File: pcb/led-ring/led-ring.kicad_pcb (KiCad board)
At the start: 2 copper layers, 30 x 30 mm, 30 parts

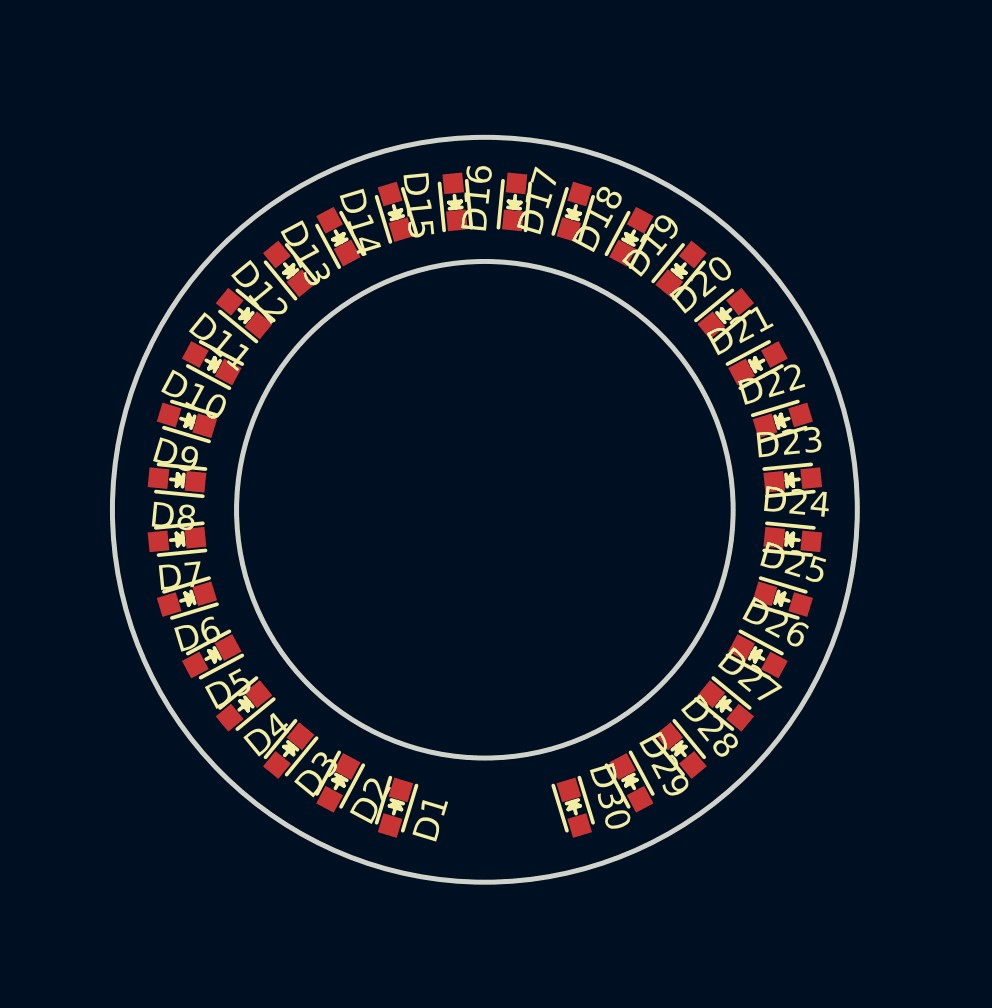
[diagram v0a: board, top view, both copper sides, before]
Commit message: o Add flat-flex footprint.
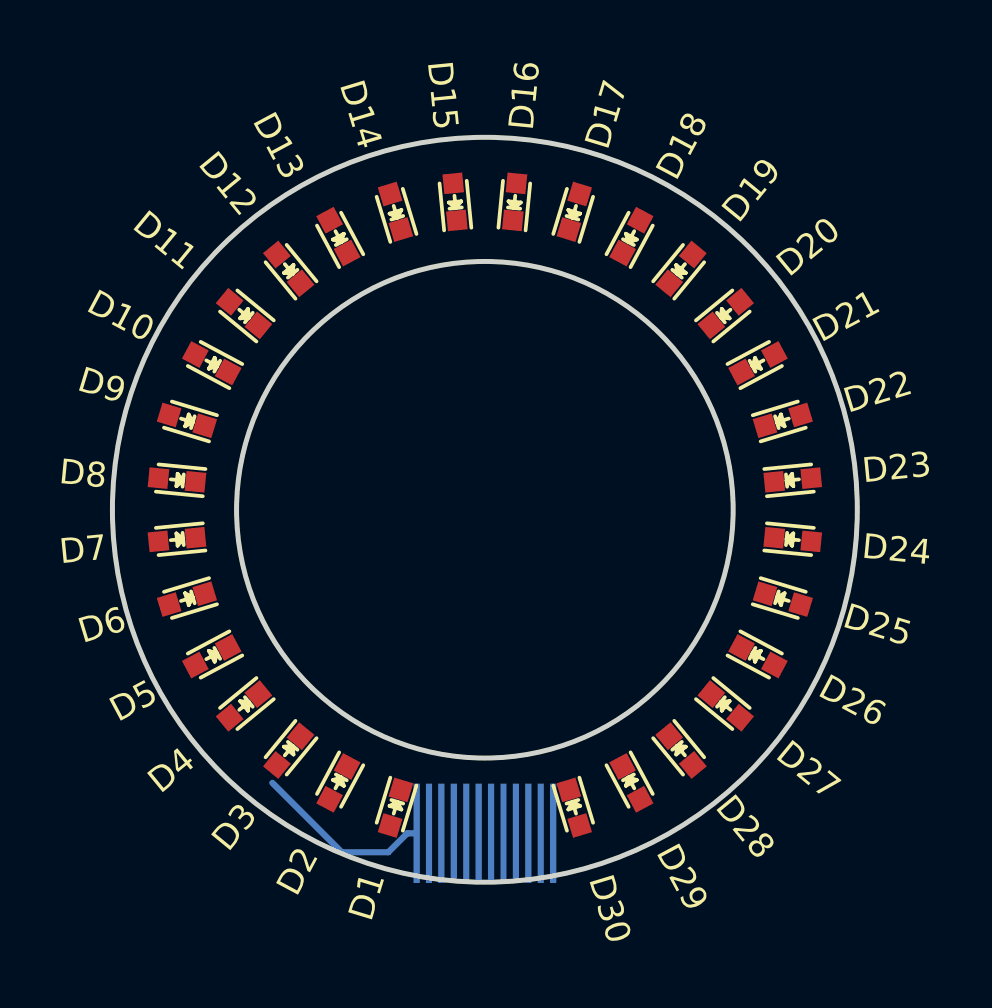
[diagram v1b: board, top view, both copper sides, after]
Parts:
- added P1: CONN_01X12, knopf:FlatFlex, B.Cu at (100.0, 113.0)
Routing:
- net A: track 0.00 -> 7.28 mm
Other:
- net class Default: clearance 0.2 -> 0.1
- rule trace_clearance: 0.2 -> 0.1

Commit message: o seed net-starts.
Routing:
- net C: track 0.00 -> 6.51 mm
- net B: track 0.00 -> 5.94 mm
- net A: track 7.28 -> 2.06 mm
- net D: track 0.00 -> 4.10 mm
- net E: track 0.00 -> 3.75 mm
- net F: track 0.00 -> 1.60 mm
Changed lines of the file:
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@@
     (links 60)
     (no_connects 60)
-    (area 84.899999 84.899999 115.100001 115.100001)
+    (area 82.586734 81.61799 118.293184 117.9685)
     (thickness 1.6)
     (drawings 2)
-    (tracks 4)
+    (tracks 25)
     (zones 0)
     (modules 31)
@@
   (gr_circle (center 100 100) (end 115 100) (layer Edge.Cuts) (width 0.2))
   (gr_circle (center 100 100) (end 110 100) (layer Edge.Cuts) (width 0.2))
-  (segment (start 94.234 113.792) (end 91.44 110.998) (width 0.25) (layer B.Cu) (net 1))
-  (segment (start 96.113 113.792) (end 94.234 113.792) (width 0.25) (layer B.Cu) (net 1))
+  (segment (start 96.113 113.792) (end 95.504 113.792) (width 0.25) (layer B.Cu) (net 1))
   (segment (start 97.25 113.03) (end 96.875 113.03) (width 0.25) (layer B.Cu) (net 1))
   (segment (start 96.875 113.03) (end 96.113 113.792) (width 0.25) (layer B.Cu) (net 1))
+  (segment (start 95.854011 111.895987) (end 95.854011 112.933989) (width 0.25) (layer B.Cu) (net 2))
+  (segment (start 95.854011 112.933989) (end 95.758 113.03) (width 0.25) (layer B.Cu) (net 2))
+  (segment (start 97.163987 110.586011) (end 95.854011 111.895987) (width 0.25) (layer B.Cu) (net 2))
+  (segment (start 97.556011 110.586011) (end 97.163987 110.586011) (width 0.25) (layer B.Cu) (net 2))
+  (segment (start 97.75 113.03) (end 97.75 110.78) (width 0.25) (layer B.Cu) (net 2))
+  (segment (start 97.75 110.78) (end 97.556011 110.586011) (width 0.25) (layer B.Cu) (net 2))
+  (segment (start 95.504 111.506) (end 95.504 112.268) (width 0.25) (layer B.Cu) (net 3))
+  (segment (start 96.774 110.236) (end 95.504 111.506) (width 0.25) (layer B.Cu) (net 3))
+  (segment (start 97.706 110.236) (end 96.774 110.236) (width 0.25) (layer B.Cu) (net 3))
+  (segment (start 98.25 113.03) (end 98.25 110.78) (width 0.25) (layer B.Cu) (net 3))
+  (segment (start 98.25 110.78) (end 97.706 110.236) (width 0.25) (layer B.Cu) (net 3))
+  (segment (start 102.294 110.236) (end 103.378 110.236) (width 0.25) (layer B.Cu) (net 4))
+  (segment (start 101.75 113.03) (end 101.75 110.78) (width 0.25) (layer B.Cu) (net 4))
+  (segment (start 101.75 110.78) (end 102.294 110.236) (width 0.25) (layer B.Cu) (net 4))
+  (segment (start 103.378 111.127998) (end 103.378 111.506) (width 0.25) (layer B.Cu) (net 5))
+  (segment (start 102.25 113.03) (end 102.25 110.999998) (width 0.25) (layer B.Cu) (net 5))
+  (segment (start 102.25 110.999998) (end 102.444999 110.804999) (width 0.25) (layer B.Cu) (net 5))
+  (segment (start 102.444999 110.804999) (end 103.055001 110.804999) (width 0.25) (layer B.Cu) (net 5))
+  (segment (start 103.055001 110.804999) (end 103.378 111.127998) (width 0.25) (layer B.Cu) (net 5))
+  (segment (start 103.632 112.523) (end 103.632 112.014) (width 0.25) (layer B.Cu) (net 6))
+  (segment (start 102.75 113.03) (end 103.125 113.03) (width 0.25) (layer B.Cu) (net 6))
+  (segment (start 103.125 113.03) (end 103.632 112.523) (width 0.25) (layer B.Cu) (net 6))
 )

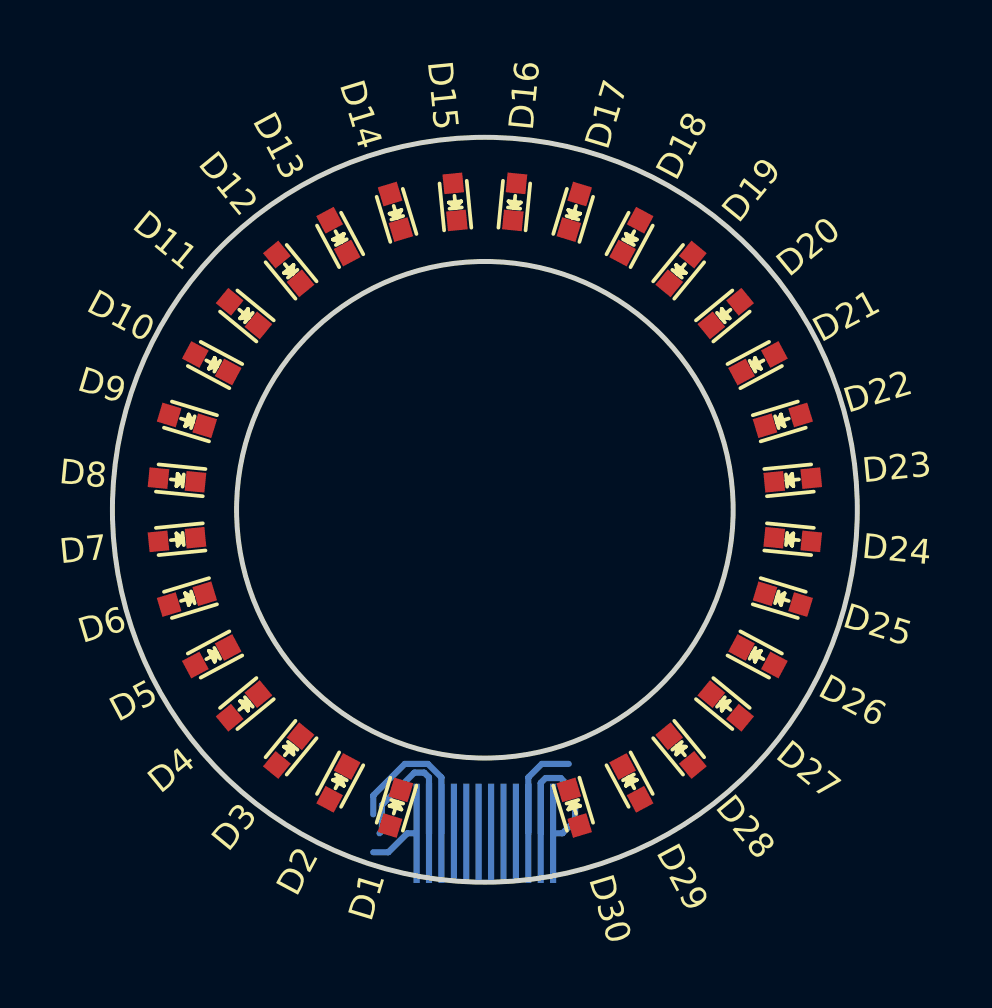
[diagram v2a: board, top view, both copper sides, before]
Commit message: o Get polygons started. Wired up first couple of LEDs.
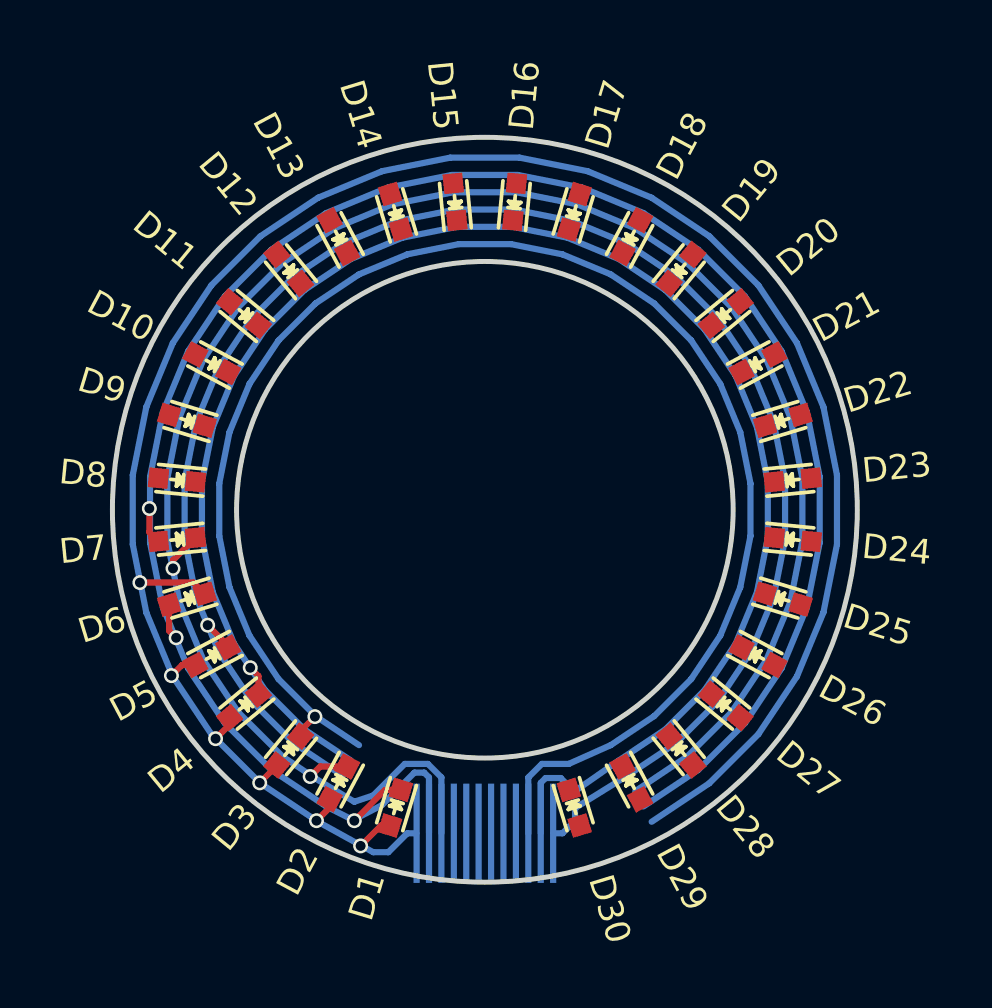
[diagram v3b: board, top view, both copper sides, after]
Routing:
- net A: track 2.06 -> 88.9 mm, vias 0 -> 6
- net B: track 5.94 -> 84.5 mm, vias 0 -> 3
- net C: track 6.51 -> 78.8 mm, vias 0 -> 2
- net F: track 1.60 -> 69.6 mm, vias 0 -> 1
- net E: track 3.75 -> 68.0 mm, vias 0 -> 1
- net D: track 4.10 -> 63.9 mm, vias 0 -> 1

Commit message: o Wire up LEDs.
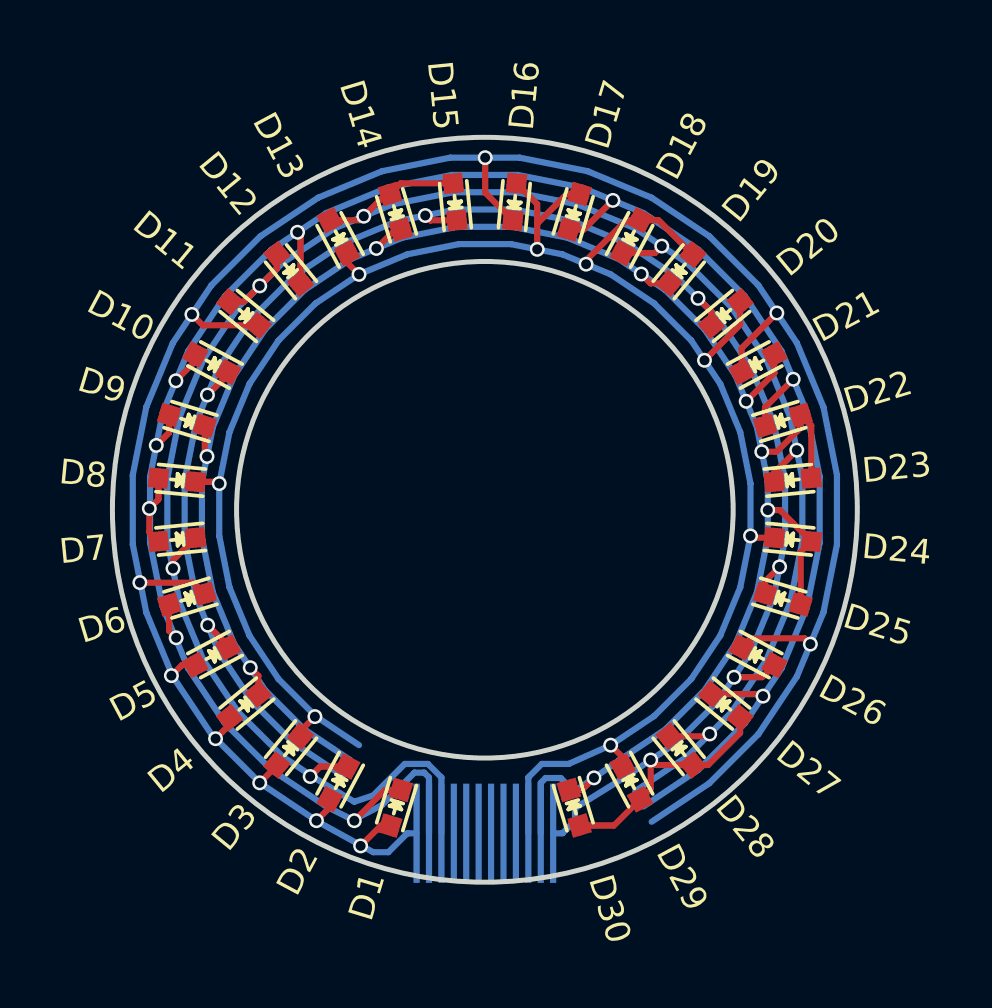
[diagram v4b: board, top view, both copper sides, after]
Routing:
- net D: track 63.9 -> 81.8 mm, vias 1 -> 8
- net E: track 68.0 -> 85.6 mm, vias 1 -> 8
- net F: track 69.6 -> 86.2 mm, vias 1 -> 7
- net C: track 78.8 -> 92.4 mm, vias 2 -> 7
- net B: track 84.5 -> 97.5 mm, vias 3 -> 9
- net A: track 88.9 -> 100.7 mm, vias 6 -> 10
